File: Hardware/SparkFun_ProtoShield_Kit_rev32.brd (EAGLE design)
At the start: 53.3 x 68.6 mm, 29 parts

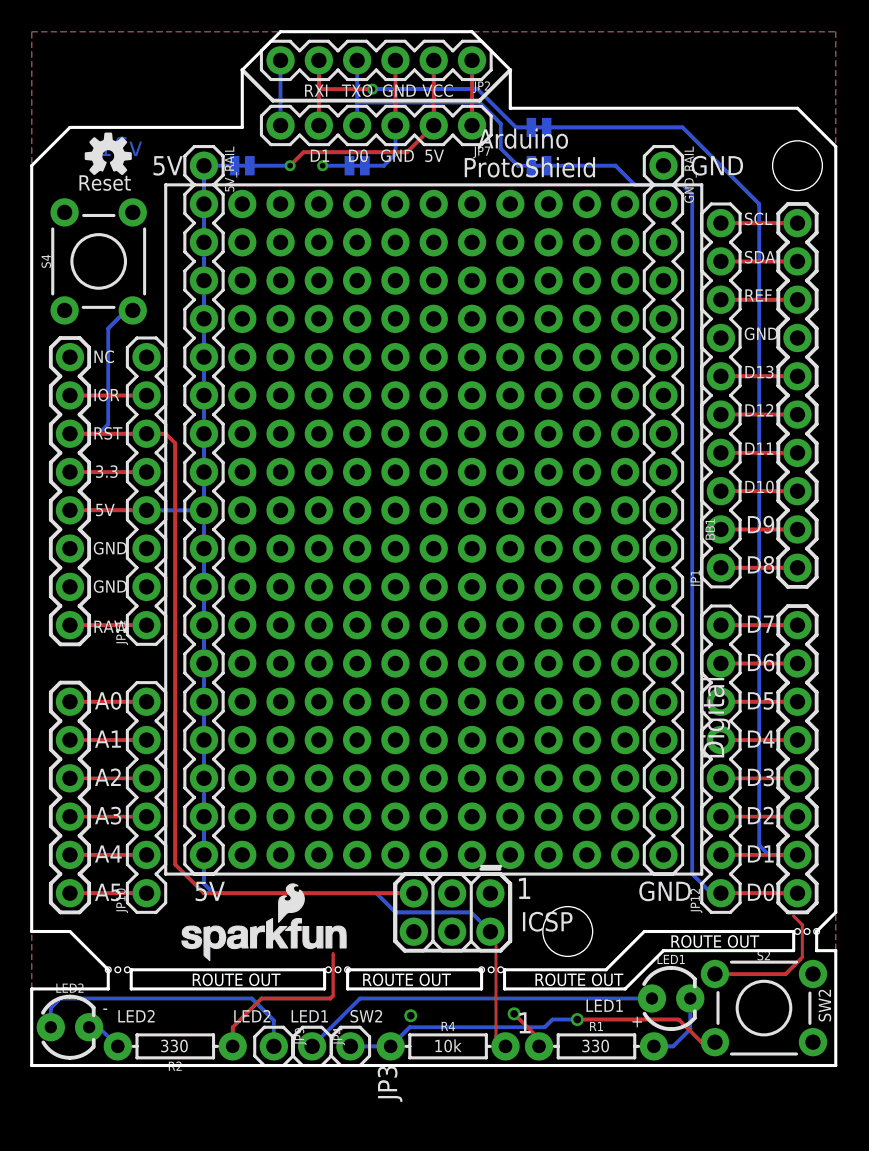
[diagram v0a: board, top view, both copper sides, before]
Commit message: Update_Proto2
-Shifted the mini-breadboard footprint
-Moved Vcc and GND rails to bottom for access
-Added VDD as an option
-Added Disconnected Breadboard rails based on Jim’s Design (GPS Shield), best of both worlds
-Add 2x more through hole pins for prototyping area
-Shifted Prototyping Hardware Around
-Switch Hardware Serial to Software -Serial to prevent bricking UART device
-Added Vcc and GND traces through mouse bite just in case
-Adjusted Header D8-SCL  so that the shield can stack with a breadboard (Michelle’s Suggestion)
-Added little bit more silkscreen to distinguish location of stackable headers
-Moved Reset button up for better access
-Switched Momentary Push Button Package to Double PTH
-Update Schematic
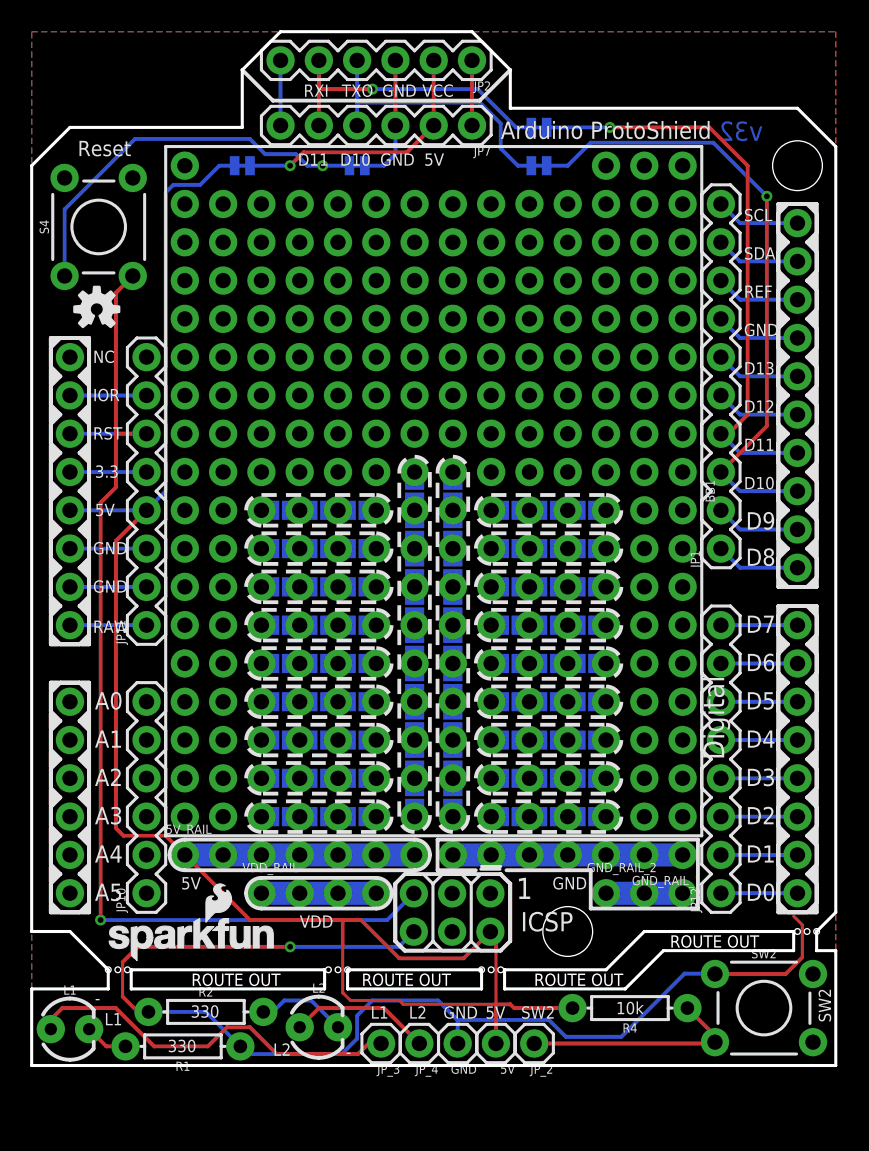
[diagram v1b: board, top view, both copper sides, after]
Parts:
- removed GND_RAIL: (no value), SparkFun-Connectors:1X19
- removed JP3, JP4, JP9: (no value), SparkFun-Connectors:1X01
- removed LED1, LED2: (no value), SparkFun-LED:LED_3MM
- removed S2: MOMENTARY-SWITCH-SPST-PTH-6.0MM-KIT, SparkFun-Switches:TACTILE_SWITCH_PTH_6.0MM_KIT
- added 5V, GND, JP_2, JP_3, JP_4: (no value), SparkFun-Connectors:1X01
- added GND_RAIL_1: (no value), SparkFun-Connectors:1X07_NO_SILK
- added GND_RAIL_2: (no value), SparkFun-Connectors:1X03_NO_SILK
- added JP13, JP14, JP15: D_RAIL1, SparkFun-Jumpers:SMT-JUMPER_2_NO_NO-SILK
- added JP16, JP17, JP18: D_RAIL2, SparkFun-Jumpers:SMT-JUMPER_2_NO_NO-SILK
- added JP19, JP20, JP21: D_RAIL3, SparkFun-Jumpers:SMT-JUMPER_2_NO_NO-SILK
- added JP22, JP23, JP24: D_RAIL4, SparkFun-Jumpers:SMT-JUMPER_2_NO_NO-SILK
- added JP25, JP26, JP27: D_RAIL5, SparkFun-Jumpers:SMT-JUMPER_2_NO_NO-SILK
- added JP28, JP29, JP30: D_RAIL6, SparkFun-Jumpers:SMT-JUMPER_2_NO_NO-SILK
- added JP31, JP32, JP33: D_RAIL7, SparkFun-Jumpers:SMT-JUMPER_2_NO_NO-SILK
- added JP34, JP35, JP36: D_RAIL8, SparkFun-Jumpers:SMT-JUMPER_2_NO_NO-SILK
- added JP37, JP38, JP39: D_RAIL9, SparkFun-Jumpers:SMT-JUMPER_2_NO_NO-SILK
- added JP40, JP41, JP42, JP43, JP44, JP45, JP46, JP47, JP48: D_RAIL18, SparkFun-Jumpers:SMT-JUMPER_2_NO_NO-SILK
- added JP49, JP50, JP51: D_RAIL17, SparkFun-Jumpers:SMT-JUMPER_2_NO_NO-SILK
- added JP52, JP53, JP54: D_RAIL16, SparkFun-Jumpers:SMT-JUMPER_2_NO_NO-SILK
- added JP55, JP56, JP57: D_RAIL15, SparkFun-Jumpers:SMT-JUMPER_2_NO_NO-SILK
- added JP58, JP59, JP60: D_RAIL14, SparkFun-Jumpers:SMT-JUMPER_2_NO_NO-SILK
- added JP61, JP62, JP63: D_RAIL13, SparkFun-Jumpers:SMT-JUMPER_2_NO_NO-SILK
- added JP64, JP65, JP66: D_RAIL12, SparkFun-Jumpers:SMT-JUMPER_2_NO_NO-SILK
- added JP67, JP68, JP69, JP70, JP71, JP72, JP73, JP74, JP75: D_RAIL10, SparkFun-Jumpers:SMT-JUMPER_2_NO_NO-SILK
- added JP76, JP77, JP78, JP79, JP80, JP81, JP82, JP83, JP84: D_RAIL11, SparkFun-Jumpers:SMT-JUMPER_2_NO_NO-SILK
- added L1, L2: (no value), SparkFun-LED:LED_3MM
- added SW2: MOMENTARY-SWITCH-SPST-PTH-6.0MM, SparkFun-Switches:TACTILE_SWITCH_PTH_6.0MM
- added VDD_RAIL: (no value), SparkFun-Connectors:1X04_NO_SILK
- 5V_RAIL: device SparkFun-Connectors:1X19 -> SparkFun-Connectors:1X07_NO_SILK
- S4: value MOMENTARY-SWITCH-SPST-PTH-6.0MM-KIT -> MOMENTARY-SWITCH-SPST-PTH-6.0MM; device SparkFun-Switches:TACTILE_SWITCH_PTH_6.0MM_KIT -> SparkFun-Switches:TACTILE_SWITCH_PTH_6.0MM
- moved 5V_RAIL 45.7 mm to (10.2, 14.0), turned to 0 degrees
- moved R1 27.4 mm to (10.0, 1.27), turned to 180 degrees
- moved R4 12.3 mm to (39.7, 3.81), turned to 180 degrees
- moved LOGO1 10.2 mm to (4.32, 50.2)
- moved U$1 4.83 mm to (4.70, 6.86)
- moved R2 3.06 mm to (11.6, 3.56), turned to 0 degrees
- moved BB1 2.54 mm to (26.7, 38.1)
- moved S4 2.29 mm to (4.45, 55.6)
- moved JP1 1.27 mm to (45.7, 34.3)
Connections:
- net A0 renamed N$2
- net A3 renamed N$4
- net A4 renamed N$3
- removed net BUTTON: JP3.1, R4.P$1, S2.3
- removed net LED1: JP4.1, LED1.A
- removed net LED2: JP9.1, LED2.A
- new net D2_NC: JP_2.1, R4.P$1, SW2.3
- new net JP3: JP_3.1, L1.A
- new net JP4: JP_4.1, L2.A
- new net VDD: VDD_RAIL.1, VDD_RAIL.2, VDD_RAIL.3
- net 5V: now also 5V.1; no longer 5V_RAIL.10, 5V_RAIL.11, 5V_RAIL.12, 5V_RAIL.13, 5V_RAIL.14, 5V_RAIL.15, 5V_RAIL.16, 5V_RAIL.17, 5V_RAIL.18, 5V_RAIL.19, 5V_RAIL.8, 5V_RAIL.9
- net D10: now also SJ2.2
- net D11: now also SJ1.2
- net GND: now also GND.1, GND_RAIL_1.1, GND_RAIL_1.2, GND_RAIL_1.3, GND_RAIL_1.4, GND_RAIL_1.5, GND_RAIL_1.6, GND_RAIL_1.7, GND_RAIL_2.1, GND_RAIL_2.2, GND_RAIL_2.3, SW2.1; no longer GND_RAIL.1, GND_RAIL.10, GND_RAIL.11, GND_RAIL.12, GND_RAIL.13, GND_RAIL.14, GND_RAIL.15, GND_RAIL.16, GND_RAIL.17, GND_RAIL.18, GND_RAIL.19, GND_RAIL.2, GND_RAIL.3, GND_RAIL.4, GND_RAIL.5, GND_RAIL.6, GND_RAIL.7, GND_RAIL.8, GND_RAIL.9, S2.1
- net N$6: now also L1.K; no longer LED1.K
- net N$7: now also L2.K; no longer LED2.K
- net RX: no longer SJ2.2
- net TX: no longer SJ1.2
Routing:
- net GND: track 34.0 -> 149.9 mm, vias 3 -> 2
- net TX: track 66.6 -> 6.98 mm
- net RX: track 63.7 -> 6.35 mm
- net 5V: track 86.9 -> 126.3 mm
- net D10: track 5.08 -> 41.9 mm, vias 0 -> 1
- net D11: track 5.08 -> 38.8 mm, vias 0 -> 1
- net BUTTON: track 25.5 -> 0.00 mm, vias 1 -> 0
- net JP3: track 0.00 -> 25.5 mm
- net LED1: track 23.9 -> 0.00 mm
- net LED2: track 18.6 -> 0.00 mm
- net D2_NC: track 0.00 -> 15.0 mm
- net JP4: track 0.00 -> 9.44 mm
- net RESET: track 63.1 -> 72.2 mm, vias 0 -> 1
- net VDD: track 0.00 -> 7.62 mm
- net N$4: track 5.08 -> 0.00 mm
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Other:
- board text added: "L1"
- board text added: "L2"
- board text added: "VDD"
- board text added: "v32"
- board text removed: "+"
- board text removed: "LED1"
- board text removed: "LED2"
- board text removed: "RX"
- board text removed: "TX"
- board text removed: "v31"

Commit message: Proto 2 QC Update
-Adjust normally open (NO) jumper pad rails so the silkscreen is not over the vias to prevent errors.
-Adjust the "+" 5V trace intersection for the prototyping hardware.
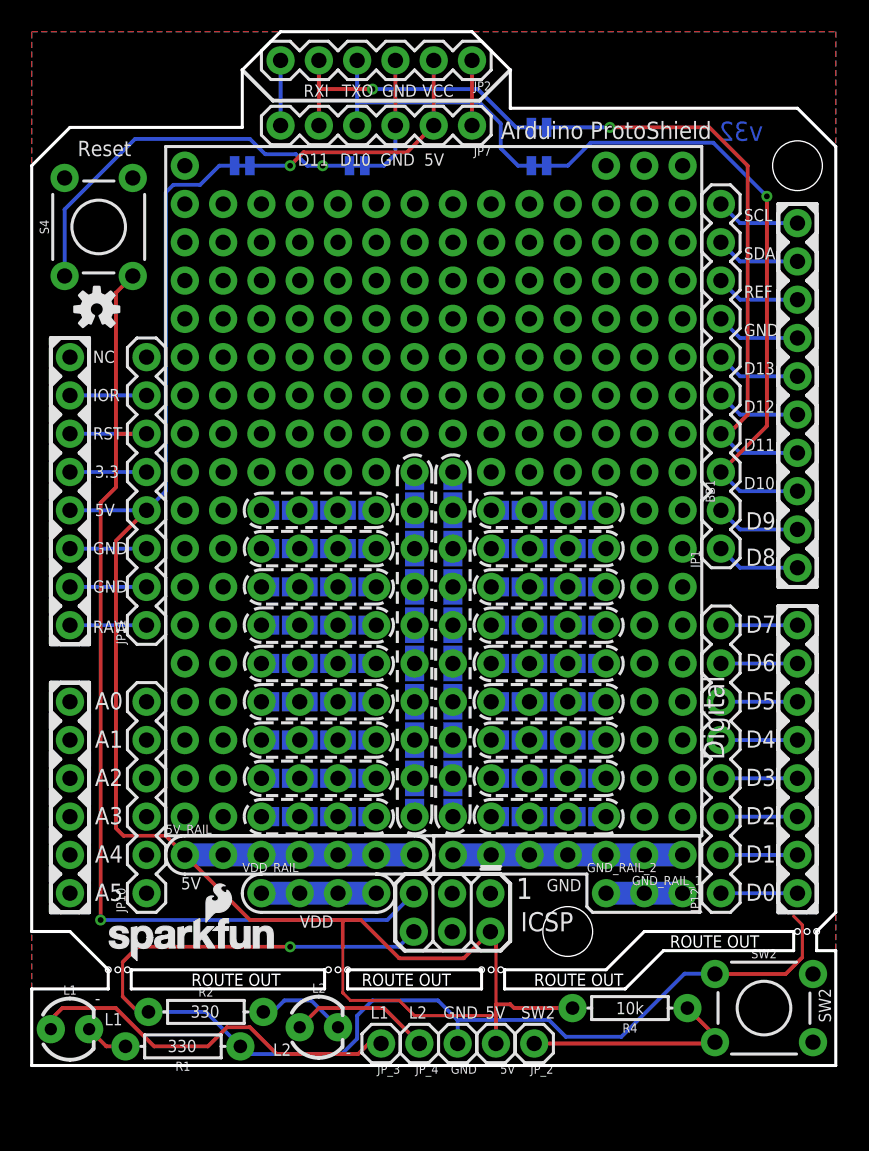
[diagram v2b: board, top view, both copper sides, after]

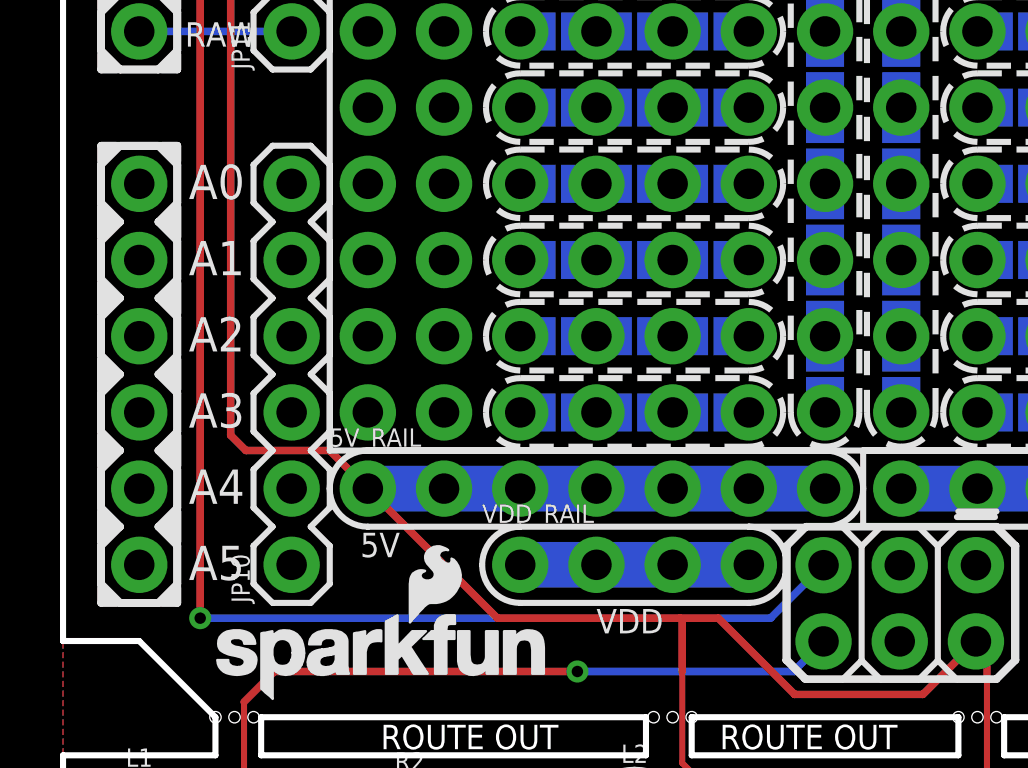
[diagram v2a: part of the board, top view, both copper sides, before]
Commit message: Airwires
-Fix airwires on analog pins, 5V rail, and VDD rail.
-Fix tiny floating net wire in schematic.
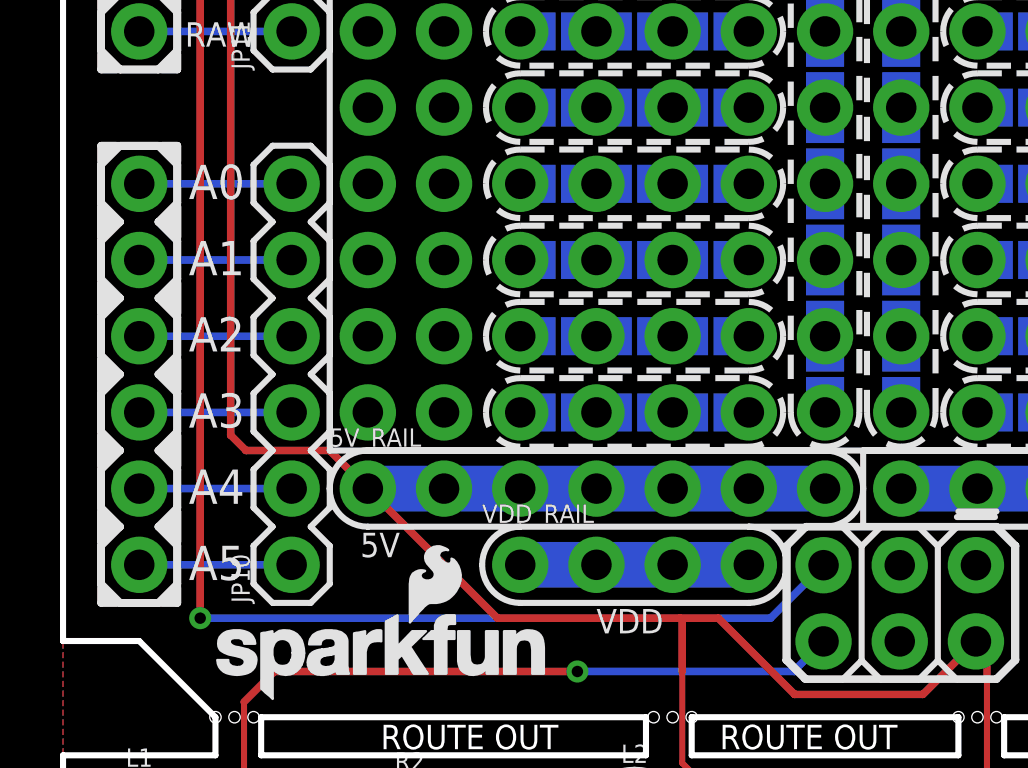
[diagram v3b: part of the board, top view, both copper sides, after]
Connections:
- net VDD: now also VDD_RAIL.4
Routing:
- net N$4: track 0.00 -> 5.08 mm
- net N$3: track 0.00 -> 5.08 mm
- net N$2: track 0.00 -> 5.08 mm
- net A5: track 0.00 -> 5.08 mm
- net A2: track 0.00 -> 5.08 mm
- net A1: track 0.00 -> 5.08 mm
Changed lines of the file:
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@@
 <layer number="39" name="tKeepout" color="4" fill="11" visible="no" active="yes"/>
 <layer number="40" name="bKeepout" color="1" fill="11" visible="no" active="yes"/>
-<layer number="41" name="tRestrict" color="4" fill="10" visible="no" active="yes"/>
-<layer number="42" name="bRestrict" color="1" fill="10" visible="no" active="yes"/>
+<layer number="41" name="tRestrict" color="4" fill="10" visible="yes" active="yes"/>
+<layer number="42" name="bRestrict" color="1" fill="10" visible="yes" active="yes"/>
 <layer number="43" name="vRestrict" color="2" fill="10" visible="no" active="yes"/>
-<layer number="44" name="Drills" color="7" fill="1" visible="no" active="yes"/>
+<layer number="44" name="Drills" color="7" fill="1" visible="yes" active="yes"/>
 <layer number="45" name="Holes" color="7" fill="1" visible="yes" active="yes"/>
 <layer number="46" name="Milling" color="3" fill="1" visible="no" active="yes"/>
-<layer number="47" name="Measures" color="7" fill="1" visible="no" active="yes"/>
+<layer number="47" name="Measures" color="7" fill="1" visible="yes" active="yes"/>
 <layer number="48" name="Document" color="7" fill="1" visible="no" active="yes"/>
 <layer number="49" name="Reference" color="7" fill="1" visible="no" active="yes"/>
@@
 <contactref element="5V_RAIL" pad="2"/>
 <contactref element="5V_RAIL" pad="1"/>
-<wire x1="10.16" y1="13.97" x2="25.4" y2="13.97" width="1.524" layer="16"/>
 <wire x1="10.16" y1="13.97" x2="14.478" y2="9.652" width="0.254" layer="1"/>
 <wire x1="14.478" y1="9.652" x2="20.574" y2="9.652" width="0.254" layer="1"/>
@@
 <wire x1="24.384" y1="4.318" x2="25.4" y2="3.302" width="0.2032" layer="1"/>
 <wire x1="32.004" y1="3.81" x2="35.8775" y2="3.81" width="0.254" layer="1"/>
-<wire x1="20.32" y1="13.97" x2="22.86" y2="13.97" width="0" layer="19" extent="1-1"/>
-<wire x1="17.78" y1="13.97" x2="20.32" y2="13.97" width="0" layer="19" extent="1-1"/>
-<wire x1="15.24" y1="13.97" x2="17.78" y2="13.97" width="0" layer="19" extent="1-1"/>
-<wire x1="12.7" y1="13.97" x2="15.24" y2="13.97" width="0" layer="19" extent="1-1"/>
-<wire x1="25.4" y1="13.97" x2="22.86" y2="13.97" width="0" layer="19" extent="1-1"/>
 <wire x1="32.004" y1="3.81" x2="31.75" y2="4.064" width="0.254" layer="1"/>
 <wire x1="31.75" y1="4.064" x2="30.7975" y2="4.064" width="0.254" layer="1"/>
 <wire x1="25.4" y1="3.302" x2="30.734" y2="3.302" width="0.2032" layer="1"/>
+<wire x1="10.16" y1="13.97" x2="12.7" y2="13.97" width="1.524" layer="16"/>
+<wire x1="12.7" y1="13.97" x2="15.24" y2="13.97" width="1.524" layer="16"/>
+<wire x1="15.24" y1="13.97" x2="17.78" y2="13.97" width="1.524" layer="16"/>
+<wire x1="17.78" y1="13.97" x2="20.32" y2="13.97" width="1.524" layer="16"/>
+<wire x1="20.32" y1="13.97" x2="22.86" y2="13.97" width="1.524" layer="16"/>
+<wire x1="22.86" y1="13.97" x2="25.4" y2="13.97" width="1.524" layer="16"/>
 </signal>
 <signal name="N$18">
@@
 <contactref element="JP8" pad="A1"/>
 <contactref element="JP10" pad="5"/>
-<wire x1="2.54" y1="21.59" x2="7.62" y2="21.59" width="0" layer="19" extent="1-1"/>
+<wire x1="2.54" y1="21.59" x2="7.62" y2="21.59" width="0.254" layer="16"/>
 </signal>
 <signal name="A2">
 <contactref element="JP8" pad="A2"/>
 <contactref element="JP10" pad="4"/>
-<wire x1="2.54" y1="19.05" x2="7.62" y2="19.05" width="0" layer="19" extent="1-1"/>
+<wire x1="2.54" y1="19.05" x2="7.62" y2="19.05" width="0.254" layer="16"/>
 </signal>
 <signal name="A5">
 <contactref element="JP8" pad="A5"/>
 <contactref element="JP10" pad="1"/>
-<wire x1="2.54" y1="11.43" x2="7.62" y2="11.43" width="0" layer="19" extent="1-1"/>
+<wire x1="2.54" y1="11.43" x2="7.62" y2="11.43" width="0.254" layer="16"/>
 </signal>
 <signal name="N$8">
@@
 <via x="10.16" y="54.61" extent="1-16" drill="1.016" diameter="1.8796"/>
 </signal>
-<signal name="N$219">
+<signal name="N$5">
 <via x="10.16" y="57.15" extent="1-16" drill="1.016" diameter="1.8796"/>
+</signal>
+<signal name="N$219">
 <via x="10.16" y="59.69" extent="1-16" drill="1.016" diameter="1.8796"/>
-<wire x1="10.16" y1="57.15" x2="10.16" y2="59.69" width="0" layer="19" extent="1-1"/>
 </signal>
 <signal name="N$221">
@@
 <contactref element="JP8" pad="A4"/>
 <contactref element="JP10" pad="2"/>
-<wire x1="2.54" y1="13.97" x2="7.62" y2="13.97" width="0" layer="19" extent="1-1"/>
+<wire x1="2.54" y1="13.97" x2="7.62" y2="13.97" width="0.254" layer="16"/>
 </signal>
 <signal name="N$4">
 <contactref element="JP8" pad="A3"/>
 <contactref element="JP10" pad="3"/>
-<wire x1="2.54" y1="16.51" x2="7.62" y2="16.51" width="0" layer="19" extent="1-1"/>
+<wire x1="2.54" y1="16.51" x2="7.62" y2="16.51" width="0.254" layer="16"/>
 </signal>
 <signal name="N$2">
 <contactref element="JP8" pad="A0"/>
 <contactref element="JP10" pad="6"/>
-<wire x1="2.54" y1="24.13" x2="7.62" y2="24.13" width="0" layer="19" extent="1-1"/>
+<wire x1="2.54" y1="24.13" x2="7.62" y2="24.13" width="0.254" layer="16"/>
 </signal>
 <signal name="VDD">
@@
 <contactref element="VDD_RAIL" pad="2"/>
 <contactref element="VDD_RAIL" pad="1"/>
-<wire x1="15.24" y1="11.43" x2="22.86" y2="11.43" width="1.524" layer="16"/>
-<wire x1="17.78" y1="11.43" x2="20.32" y2="11.43" width="0" layer="19" extent="1-1"/>
-<wire x1="22.86" y1="11.43" x2="20.32" y2="11.43" width="0" layer="19" extent="16-16"/>
+<wire x1="15.24" y1="11.43" x2="17.78" y2="11.43" width="1.524" layer="16"/>
+<wire x1="17.78" y1="11.43" x2="20.32" y2="11.43" width="1.524" layer="16"/>
+<contactref element="VDD_RAIL" pad="4"/>
+<wire x1="20.32" y1="11.43" x2="22.86" y2="11.43" width="1.524" layer="16"/>
 </signal>
 <signal name="JP3">
